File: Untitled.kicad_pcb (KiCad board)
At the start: 2 copper layers, 37 x 37 mm, 22 parts, among them J1 Battery Connector, J2 Top Screw Terminal, J3 Bottom Screw Terminal, Q1 Q_NMOS_DGS, Q2 Q_NMOS_DGS, Q3 Q_NMOS_DGS, U1 XIAO-ESP32-S3-SMD, U3 LSM6DSO32, U4 MS5611-01BA

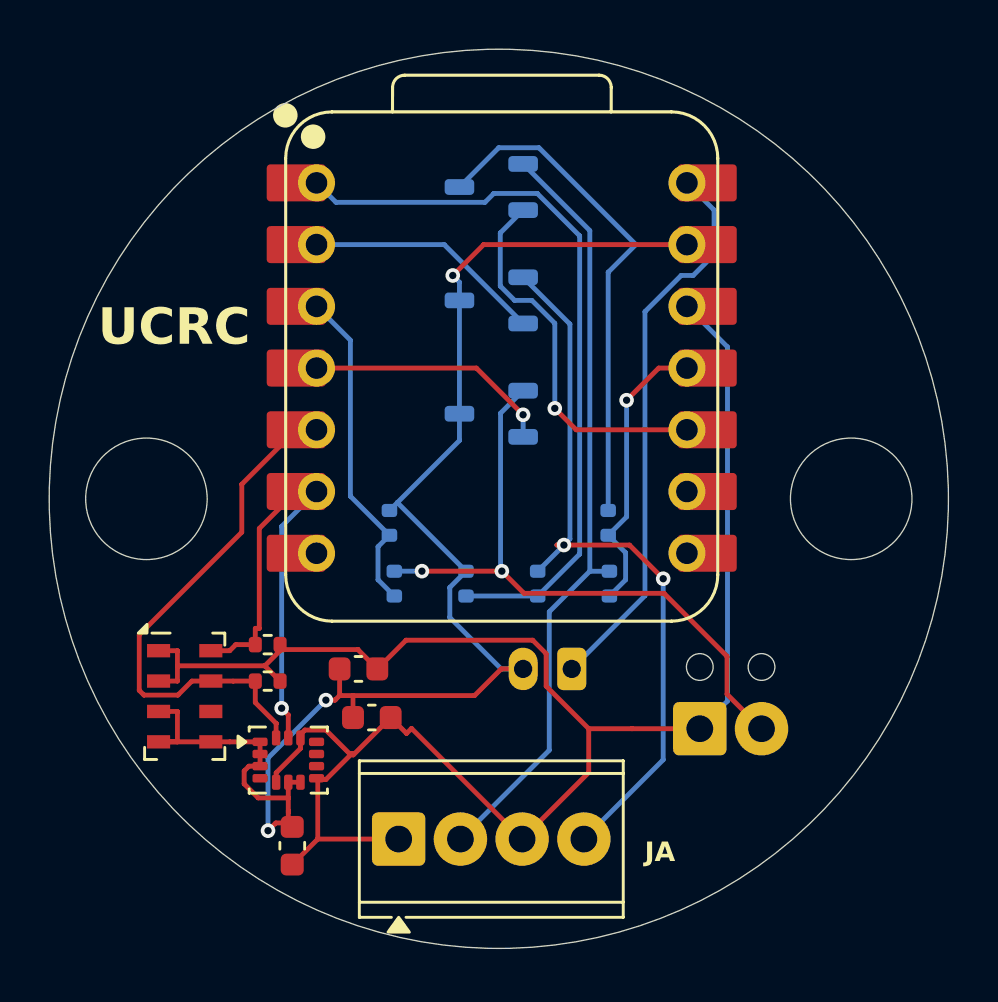
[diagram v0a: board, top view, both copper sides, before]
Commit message: I forgot to save the PCB file so it autosaved and that's alot of bloat
Also the design I did is the untitled one, the numbered untitled ones are when i was doing something weird with saving copies but doing that doesn't link it to the schematic file.
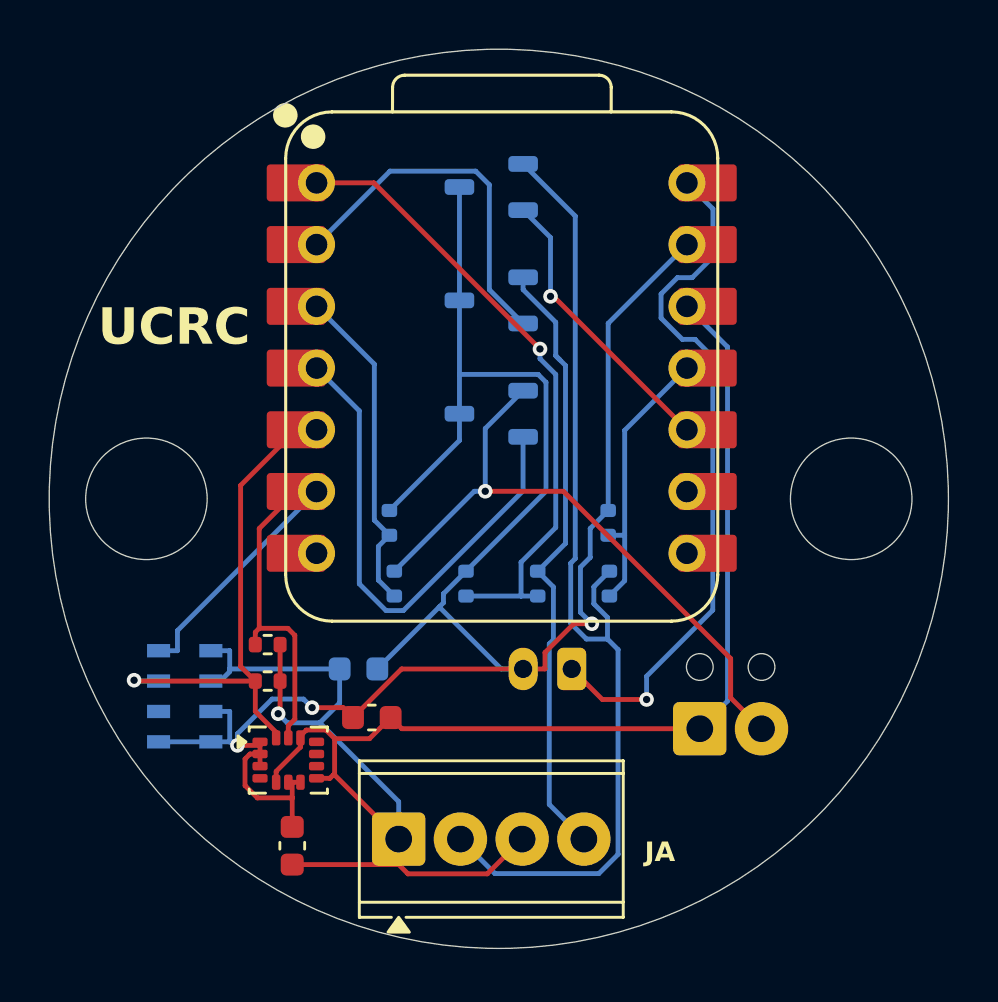
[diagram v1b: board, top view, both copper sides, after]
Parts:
- C3, U4: moved to B.Cu
- turned C3 to 180 degrees
- turned U4 to 180 degrees
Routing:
- net /IGNIT 3: track 11.0 -> 21.9 mm, vias 1 -> 0
- net /APPO: track 31.9 -> 41.4 mm
- net /MAIN: track 31.3 -> 25.5 mm, vias 2 -> 0
- net +BATT: track 24.0 -> 29.7 mm, vias 0 -> 1
- net /IGNIT 2: track 10.7 -> 15.7 mm
- net /CONT 2: track 31.4 -> 26.8 mm, vias 0 -> 1
- net /IGNIT 1: track 16.5 -> 12.7 mm
- net /SCL: track 20.7 -> 23.4 mm, vias 1 -> 0
- net +3.3V: track 77.9 -> 76.7 mm, vias 0 -> 1
- net /SDA: track 22.0 -> 21.1 mm, vias 0 -> 1
- net /CONT 1: track 12.8 -> 12.2 mm, vias 1 -> 0
- net /MOTOR: track 26.8 -> 26.3 mm, vias 2 -> 1

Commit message: Added silkscreens
Added the silkscreens that have the part numbers onto the PCB Schematic. From what I understand, the silkscreens can go overtop the copper tracks because they are on different layers. If that's not the case, let me know.
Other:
- board text removed: "JA"
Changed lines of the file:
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@@
 		(tags "capacitor")
 		(property "Reference" "C1"
-			(at 0 -1.43 0)
+			(at 2.225 -1 0)
 			(layer "F.SilkS")
-			(hide yes)
 			(effects
 				(font
@@
 		(tags "resistor")
 		(property "Reference" "R1"
-			(at 0 -1.17 0)
+			(at 2.01 0 0)
 			(layer "F.SilkS")
-			(hide yes)
 			(effects
 				(font
@@
 		(tags "LGA NoLead")
 		(property "Reference" "U3"
-			(at 0 -2.2 0)
+			(at -2.8375 0.75 0)
 			(layer "F.SilkS")
-			(hide yes)
 			(effects
 				(font
@@
 		(tags "THT Terminal Block Phoenix MPT-0,5-4-2.54 pitch 2.54mm size 10.6x6.2mm drill 1.1mm pad 2.2mm")
 		(property "Reference" "J2"
-			(at 3.81 -4.22 0)
+			(at 10.62 2 0)
 			(layer "F.SilkS")
-			(hide yes)
 			(effects
 				(font
@@
 		(tags "capacitor")
 		(property "Reference" "C2"
-			(at 0 -1.43 90)
+			(at -0.275 -1.43 90)
 			(layer "F.SilkS")
-			(hide yes)
 			(effects
 				(font
@@
 		(tags "resistor")
 		(property "Reference" "R2"
-			(at 0 -1.17 0)
+			(at 2.01 0 0)
 			(layer "F.SilkS")
-			(hide yes)
 			(effects
 				(font
@@
 		(at 206.12 62.12)
 		(property "Reference" "U1"
-			(at -8 -12 0)
+			(at -5.62 -11.12 0)
 			(unlocked yes)
 			(layer "F.SilkS")
-			(hide yes)
 			(effects
 				(font
-					(size 0.635 0.635)
-					(thickness 0.1016)
+					(size 1 1)
+					(thickness 0.125)
 				)
 			)
@@
 			(at 0 1.17 90)
 			(layer "B.SilkS")
-			(hide yes)
 			(effects
 				(font
@@
 			(at 0 1.17 90)
 			(layer "B.SilkS")
-			(hide yes)
 			(effects
 				(font
@@
 			(at 0 1.17 90)
 			(layer "B.SilkS")
-			(hide yes)
 			(effects
 				(font
@@
 		(tags "lga land grid array")
 		(property "Reference" "U4"
-			(at 0 3.65 0)
+			(at -0.425 -3.875 0)
 			(layer "B.SilkS")
-			(hide yes)
 			(effects
 				(font
@@
 			(at 1.27 4.22 0)
 			(layer "B.SilkS")
-			(hide yes)
 			(effects
 				(font
@@
 		(tags "connector JST PH vertical")
 		(property "Reference" "J1"
-			(at 1 2.9 0)
+			(at 1 -4 0)
 			(layer "B.SilkS")
-			(hide yes)
 			(effects
 				(font
@@
 			(at 0 1.17 90)
 			(layer "B.SilkS")
-			(hide yes)
 			(effects
 				(font
@@
 			(at 0 1.17 90)
 			(layer "B.SilkS")
-			(hide yes)
 			(effects
 				(font
@@
 			(at 0 1.43 0)
 			(layer "B.SilkS")
-			(hide yes)
 			(effects
 				(font
@@
 		(tags "TSOT-23")
 		(property "Reference" "Q3"
-			(at 0 2.6 0)
+			(at 3.19 0 0)
 			(layer "B.SilkS")
-			(hide yes)
 			(effects
 				(font
@@
 		(tags "TSOT-23")
 		(property "Reference" "Q1"
-			(at 0 2.6 0)
+			(at 3.19 -0.33 0)
 			(layer "B.SilkS")
-			(hide yes)
 			(effects
 				(font
@@
 		(tags "TSOT-23")
 		(property "Reference" "Q2"
-			(at 0 2.6 0)
+			(at 3.19 -0.165 0)
 			(layer "B.SilkS")
-			(hide yes)
 			(effects
 				(font
@@
 			(at 0 1.17 90)
 			(layer "B.SilkS")
-			(hide yes)
 			(effects
 				(font
@@
 				(bold yes)
 			)
-			(justify left bottom)
-		)
-	)
-	(gr_text "JA"
-		(at 212 82.5 0)
-		(layer "F.SilkS")
-		(effects
-			(font
-				(size 0.8 0.8)
-				(thickness 0.16)
-				(bold yes)
-			)

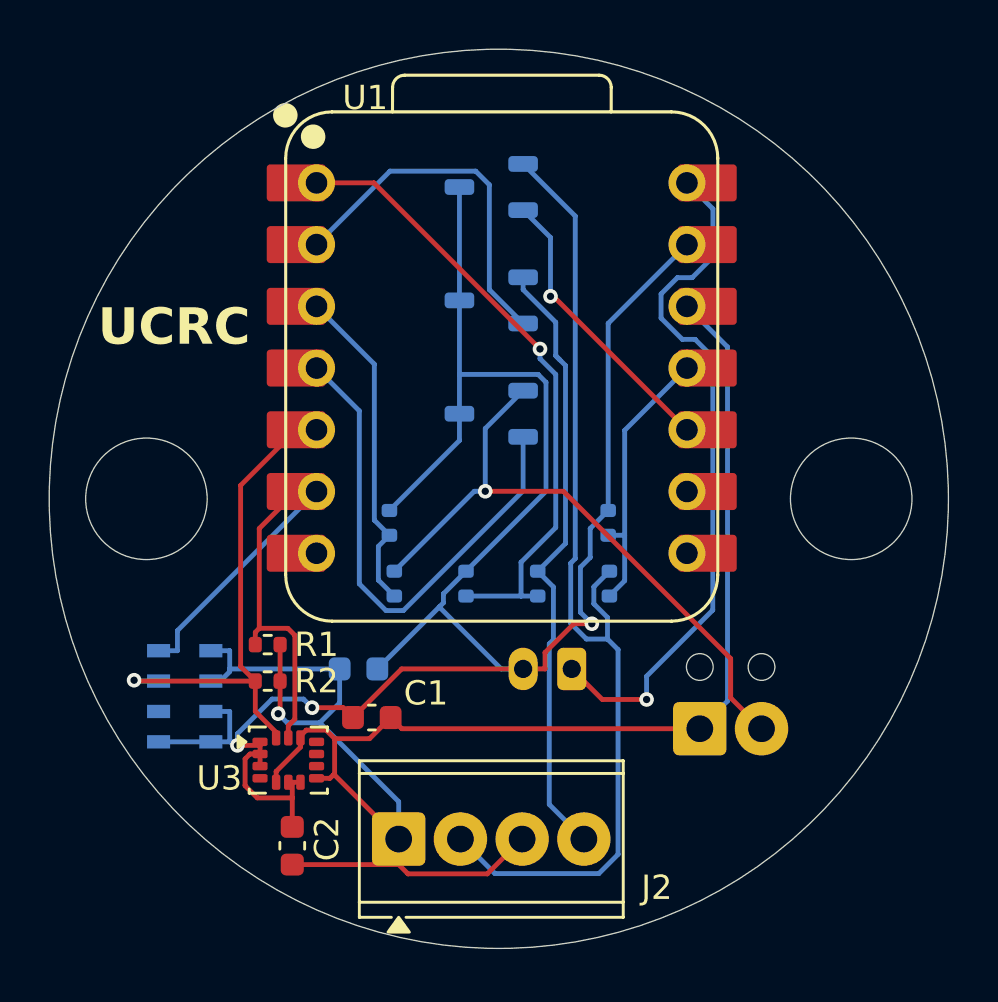
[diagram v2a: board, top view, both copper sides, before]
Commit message: Changed Mosfet pad arrangement and Screwport terminal location
Minor silksreen changes were also made.
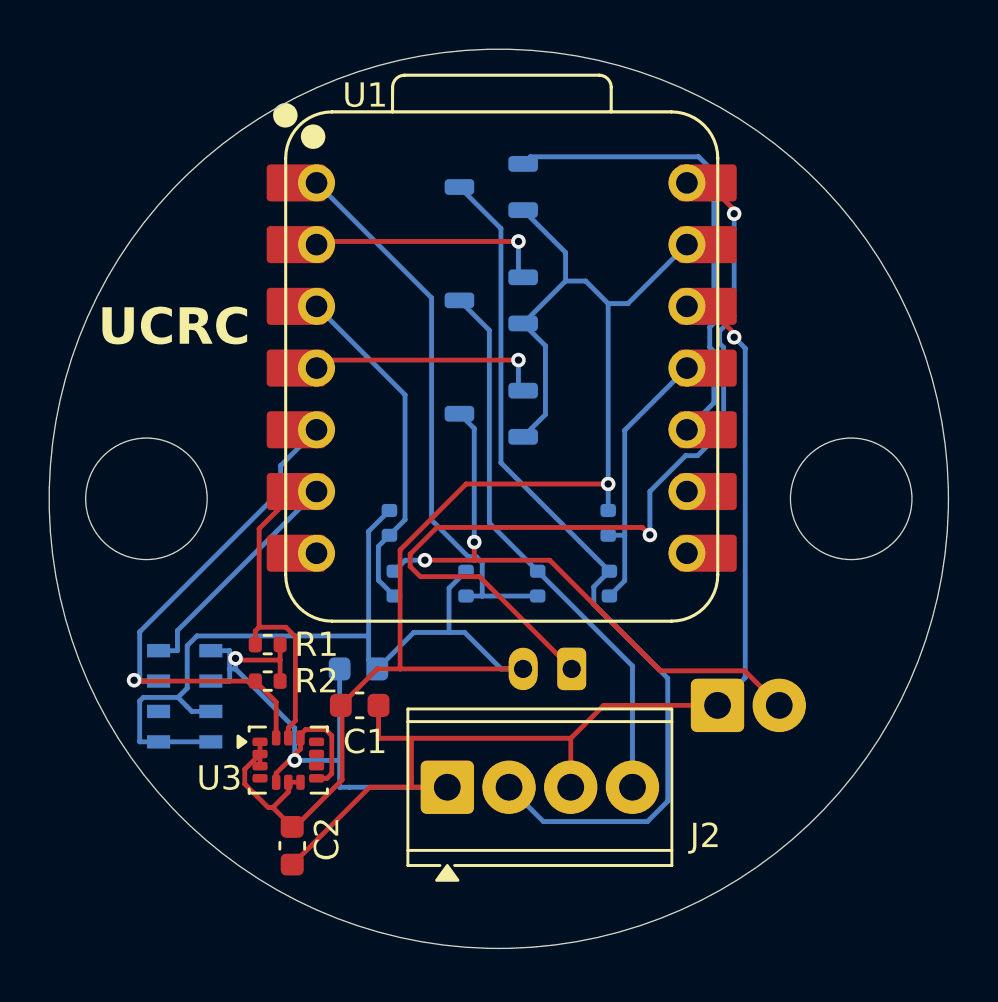
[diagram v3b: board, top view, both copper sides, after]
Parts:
- moved J2 2.92 mm to (203.9, 79.4)
- moved J3 1.21 mm to (215.0, 76.0)
- moved C1 0.71 mm to (200.3, 76.0)
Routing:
- net /IGNIT 3: track 21.9 -> 10.6 mm, vias 0 -> 1
- net -BATT: track 87.3 -> 97.7 mm, vias 3 -> 1
- net /IGNIT 1: track 12.7 -> 20.3 mm, vias 1 -> 0
- net +BATT: track 29.7 -> 37.0 mm, vias 1 -> 2
- net /IGNIT 2: track 15.7 -> 10.8 mm, vias 0 -> 1
- net /APPO: track 41.4 -> 36.8 mm
- net /CONT 2: track 26.8 -> 23.8 mm, vias 1 -> 0
- net /MAIN: track 25.5 -> 23.0 mm
- net /SDA: track 21.1 -> 22.9 mm
- net +3.3V: track 76.7 -> 75.0 mm, vias 1 -> 3
- net /MOTOR: track 26.3 -> 24.8 mm, vias 1 -> 2
- net /CONT 3: track 14.5 -> 15.0 mm

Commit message: Added cutouts, spaced rod holes
Added cutouts to the side of the PCB for wires to pass through on both sides of the ESP32. Changed distance between screw holes to accurately reflect the spacing used for threaded rods on previous avionics designs.
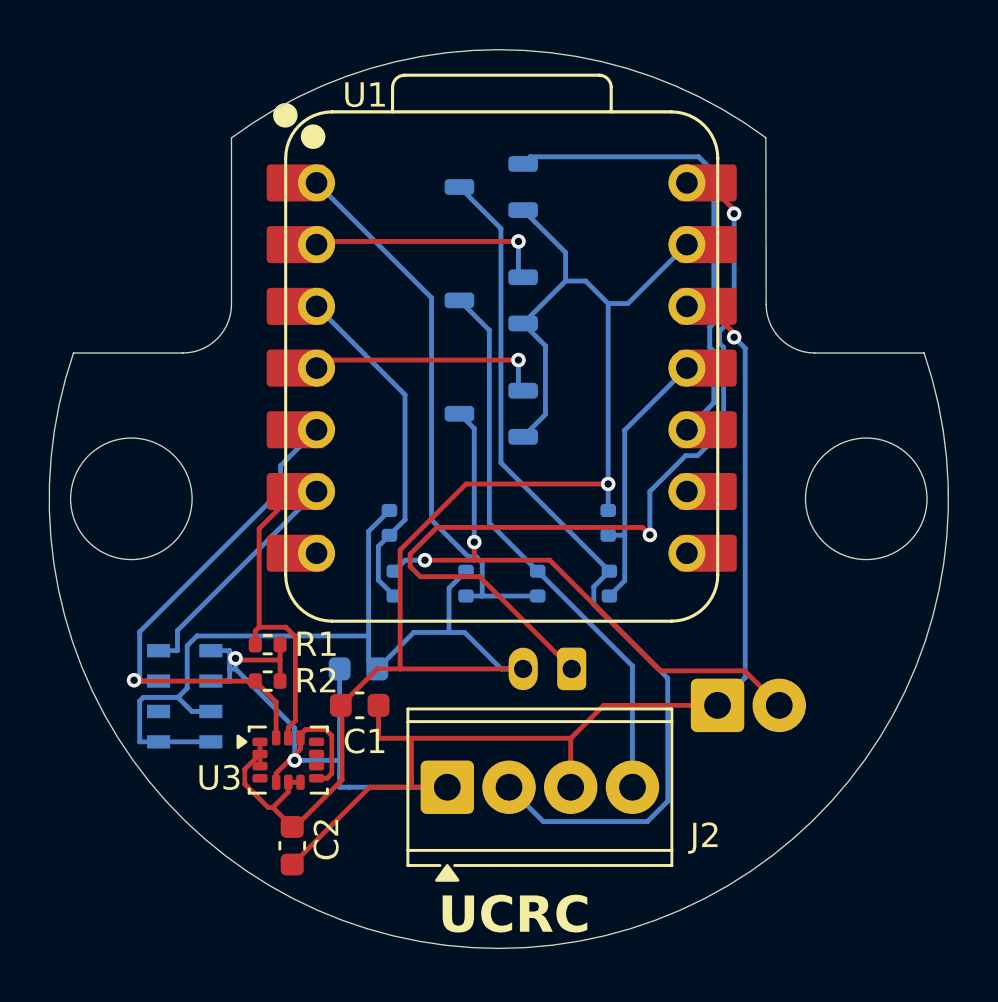
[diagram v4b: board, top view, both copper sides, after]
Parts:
- moved REF** 0.62 mm to (221.1, 67.5)
- moved Trust 0.62 mm to (190.9, 67.5)
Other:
- outline, holes or cut-outs redrawn
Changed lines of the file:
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@@
 			(plot_on_all_layers_selection 0x00000000_00000000_00000000_00000000)
 			(disableapertmacros no)
-			(usegerberextensions no)
+			(usegerberextensions yes)
 			(usegerberattributes yes)
 			(usegerberadvancedattributes yes)
-			(creategerberjobfile yes)
+			(creategerberjobfile no)
 			(dashed_line_dash_ratio 12.000000)
 			(dashed_line_gap_ratio 3.000000)
@@
 			(outputformat 1)
 			(mirror no)
-			(drillshape 1)
+			(drillshape 0)
 			(scaleselection 1)
-			(outputdirectory "")
+			(outputdirectory "../../../Downloads/")
 		)
 	)
@@
 	(footprint "MountingHole:MountingHole_5mm"
 		(layer "F.Cu")
-		(at 220.5 67.5)
+		(at 221.12 67.5)
 		(descr "Mounting Hole 5mm, no annular, generated by kicad-footprint-generator mountinghole.py")
 		(tags "mountinghole")
@@
 	(footprint "MountingHole:MountingHole_5mm"
 		(layer "F.Cu")
-		(at 191.5 67.5)
+		(at 190.88 67.5)
 		(descr "Mounting Hole 5mm, no annular, generated by kicad-footprint-generator mountinghole.py")
 		(tags "mountinghole")
@@
 		)
 	)
-	(gr_circle
-		(center 206 67.5)
-		(end 224.5 67.5)
+	(gr_line
+		(start 223.5 61.5)
+		(end 219 61.5)
 		(stroke
 			(width 0.05)
-			(type solid)
+			(type default)
+		)
+		(layer "Edge.Cuts")
+	)
+	(gr_arc
+		(start 195 59.5)
+		(mid 194.414214 60.914214)
+		(end 193 61.5)
+		(stroke
+			(width 0.05)
+			(type default)
+		)
+		(layer "Edge.Cuts")
+	)
+	(gr_arc
+		(start 195 52.65)
+		(mid 205.992724 49.019674)
+		(end 216.988303 52.641343)
+		(stroke
+			(width 0.05)
+			(type default)
+		)
+		(layer "Edge.Cuts")
+	)
+	(gr_arc
+		(start 219 61.5)
+		(mid 217.585786 60.914214)
+		(end 217 59.5)
+		(stroke
+			(width 0.05)
+			(type default)
+		)
+		(layer "Edge.Cuts")
+	)
+	(gr_line
+		(start 195 59.5)
+		(end 195 52.65)
+		(stroke
+			(width 0.05)
+			(type default)
+		)
+		(layer "Edge.Cuts")
+	)
+	(gr_line
+		(start 217 59.5)
+		(end 216.988303 52.641343)
+		(stroke
+			(width 0.05)
+			(type default)
+		)
+		(layer "Edge.Cuts")
+	)
+	(gr_arc
+		(start 223.5 61.5)
+		(mid 206 86)
+		(end 188.5 61.5)
+		(stroke
+			(width 0.05)
+			(type default)
+		)
+		(layer "Edge.Cuts")
+	)
+	(gr_line
+		(start 188.5 61.5)
+		(end 193 61.5)
+		(stroke
+			(width 0.05)
+			(type default)
 		)
-		(fill no)
 		(layer "Edge.Cuts")
 	)
 	(gr_text "UCRC"
-		(at 189.5 61.3015 0)
+		(at 203.5 85.5 0)
 		(layer "F.SilkS")
 		(effects

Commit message: Initial Routing
Completed initial manual routing of PCB traces. All nets are fully connected.
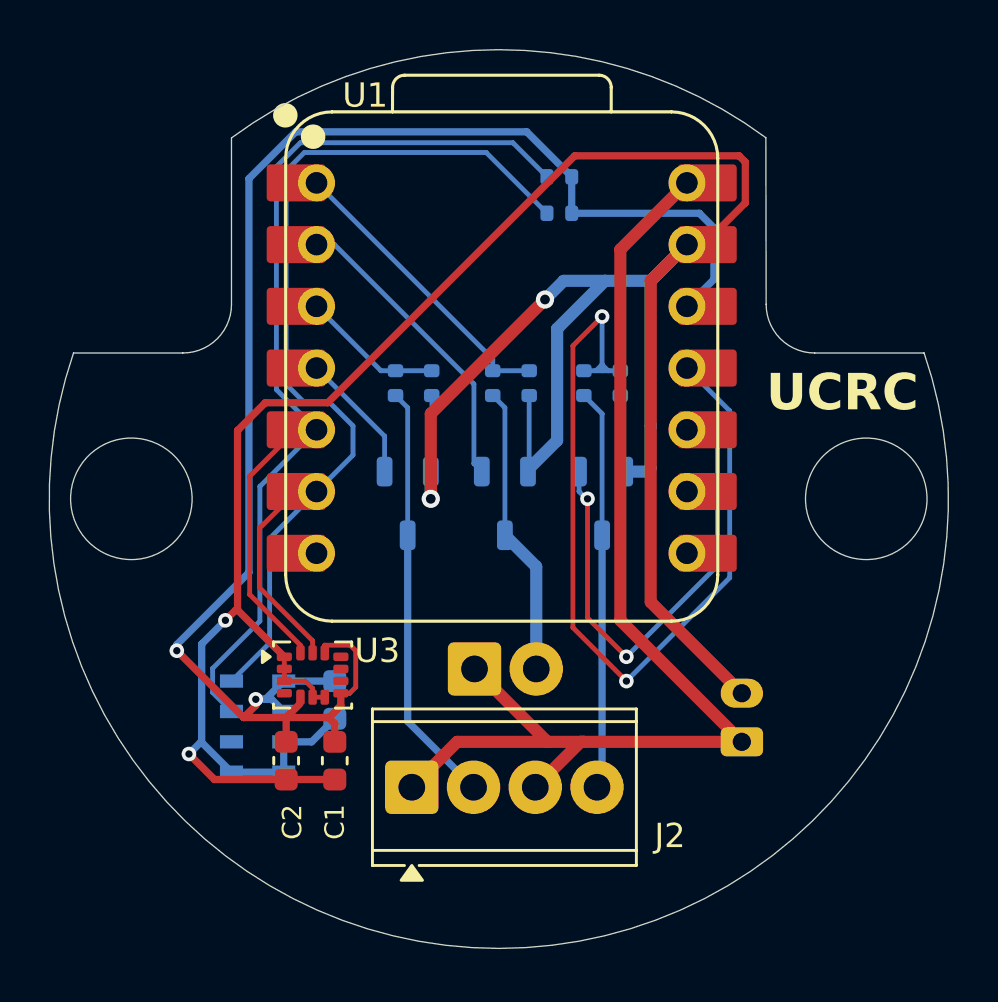
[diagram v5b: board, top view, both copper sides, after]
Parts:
- R1, R2: moved to B.Cu
- R3, R4: value 10K -> 100K
- R5: renamed from R6; value 10K -> 100K
- R6: renamed from R5; value 10K -> 100K
- R7: renamed from R8; value 10K -> 100K
- R8: renamed from R7; value 10K -> 100K
- moved R2 24.0 mm to (208.5, 54.2)
- moved R1 21.4 mm to (208.5, 55.8)
- moved Q1 13.5 mm to (202.2, 67.7), turned to -90 degrees
- moved R4 12.1 mm to (201.8, 62.7), turned to -90 degrees
- moved R5 10.4 mm to (211.0, 62.7), turned to -90 degrees
- moved J3 10.1 mm to (205.0, 74.5)
- moved Q2 9.52 mm to (210.2, 67.7), turned to -90 degrees
- moved R3 9.26 mm to (203.2, 62.7), turned to -90 degrees
- moved R8 9.19 mm to (205.8, 62.7), turned to -90 degrees
- moved R6 8.47 mm to (209.5, 62.7), turned to -90 degrees
- moved R7 8.13 mm to (207.2, 62.7), turned to -90 degrees
- moved J1 7.62 mm to (216.0, 77.5), turned to 90 degrees
- moved Q3 3.73 mm to (206.2, 67.7), turned to -90 degrees
- moved U3 3.64 mm to (198.3, 74.8)
- moved C2 3.51 mm to (197.2, 78.3), turned to 90 degrees
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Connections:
- J2 pad 1: +3.3V -> +BATT
- J2 pad 3: +3.3V -> +BATT
- J3 pad 1: +3.3V -> +BATT
- U1 pad 1: /CONT 2 -> /CONT 3
- U1 pad 10: /IGNIT 1 -> /IGNIT 2
- U1 pad 11: /CONT 1 -> /CONT 2
- U1 pad 2: /IGNIT 2 -> /IGNIT 3
- U1 pad 3: /CONT 3 -> /CONT 1
- U1 pad 4: /IGNIT 3 -> /IGNIT 1
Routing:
- net -BATT: track 97.7 -> 130.8 mm, vias 1 -> 4
- net /SDA: track 22.9 -> 48.2 mm, vias 1 -> 0
- net /SCL: track 23.5 -> 45.1 mm
- net /APPO: track 36.8 -> 17.4 mm
- net /IGNIT 1: track 20.3 -> 5.42 mm
- net /MOTOR: track 24.8 -> 12.0 mm, vias 2 -> 0
- net /CONT 2: track 23.8 -> 36.2 mm, vias 0 -> 2
- net +BATT: track 37.0 -> 47.6 mm, vias 2 -> 0
- net /IGNIT 2: track 10.8 -> 20.3 mm, vias 1 -> 2
- net +3.3V: track 75.0 -> 68.0 mm, vias 3 -> 2
- net /MAIN: track 23.0 -> 16.5 mm
- net /CONT 1: track 12.2 -> 5.84 mm
- net /CONT 3: track 15.0 -> 12.2 mm
- net /IGNIT 3: track 10.6 -> 12.6 mm, vias 1 -> 0
